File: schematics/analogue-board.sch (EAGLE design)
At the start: 81 parts, among them U1 L78S09

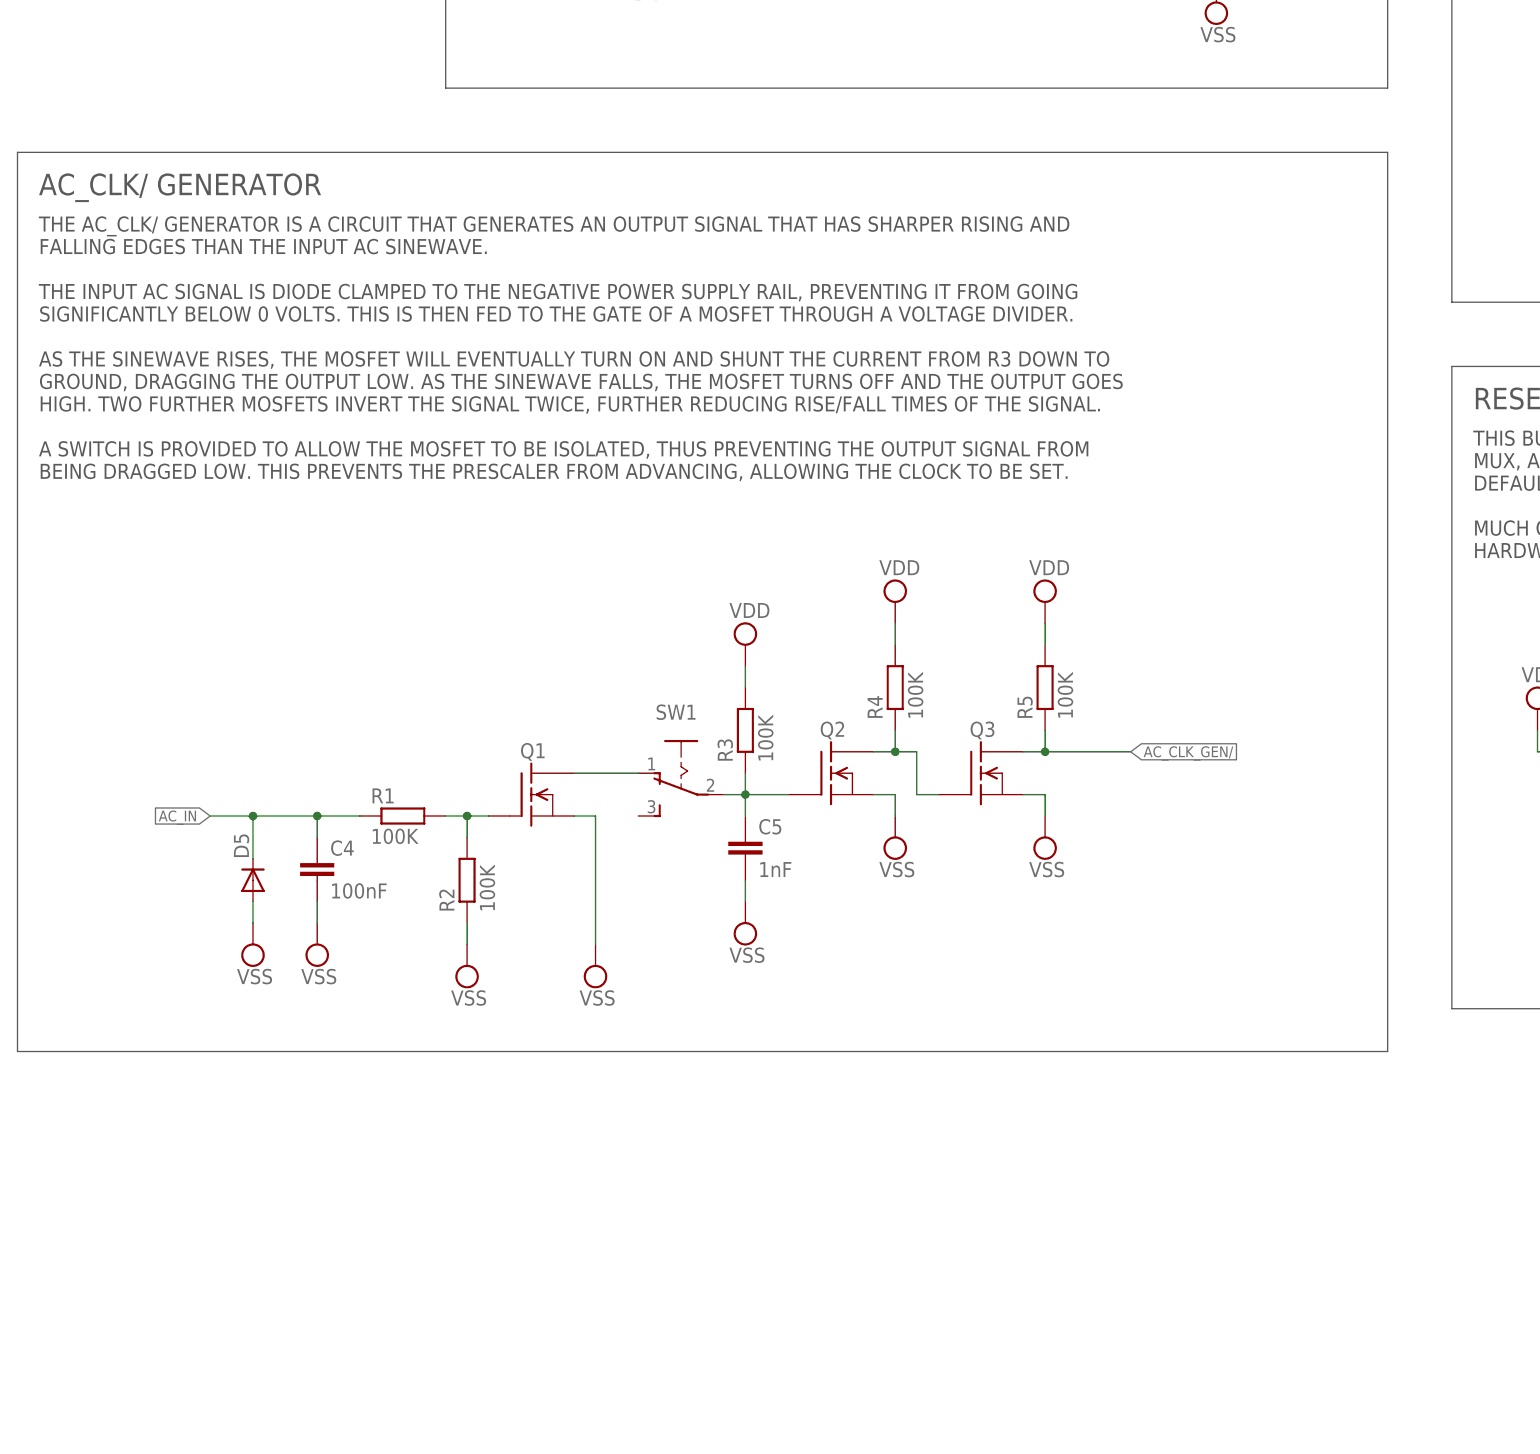
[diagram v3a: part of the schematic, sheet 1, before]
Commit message: Time module build (#7)
* Add design files (schematics) for time module.

* Upload files related to time module build.

Includes:

* revised analogue schematic to address a design fault
* C program used to collect offset statistics

* Rename directory for offset monitor program, its not a "script"

* Finalise README.md
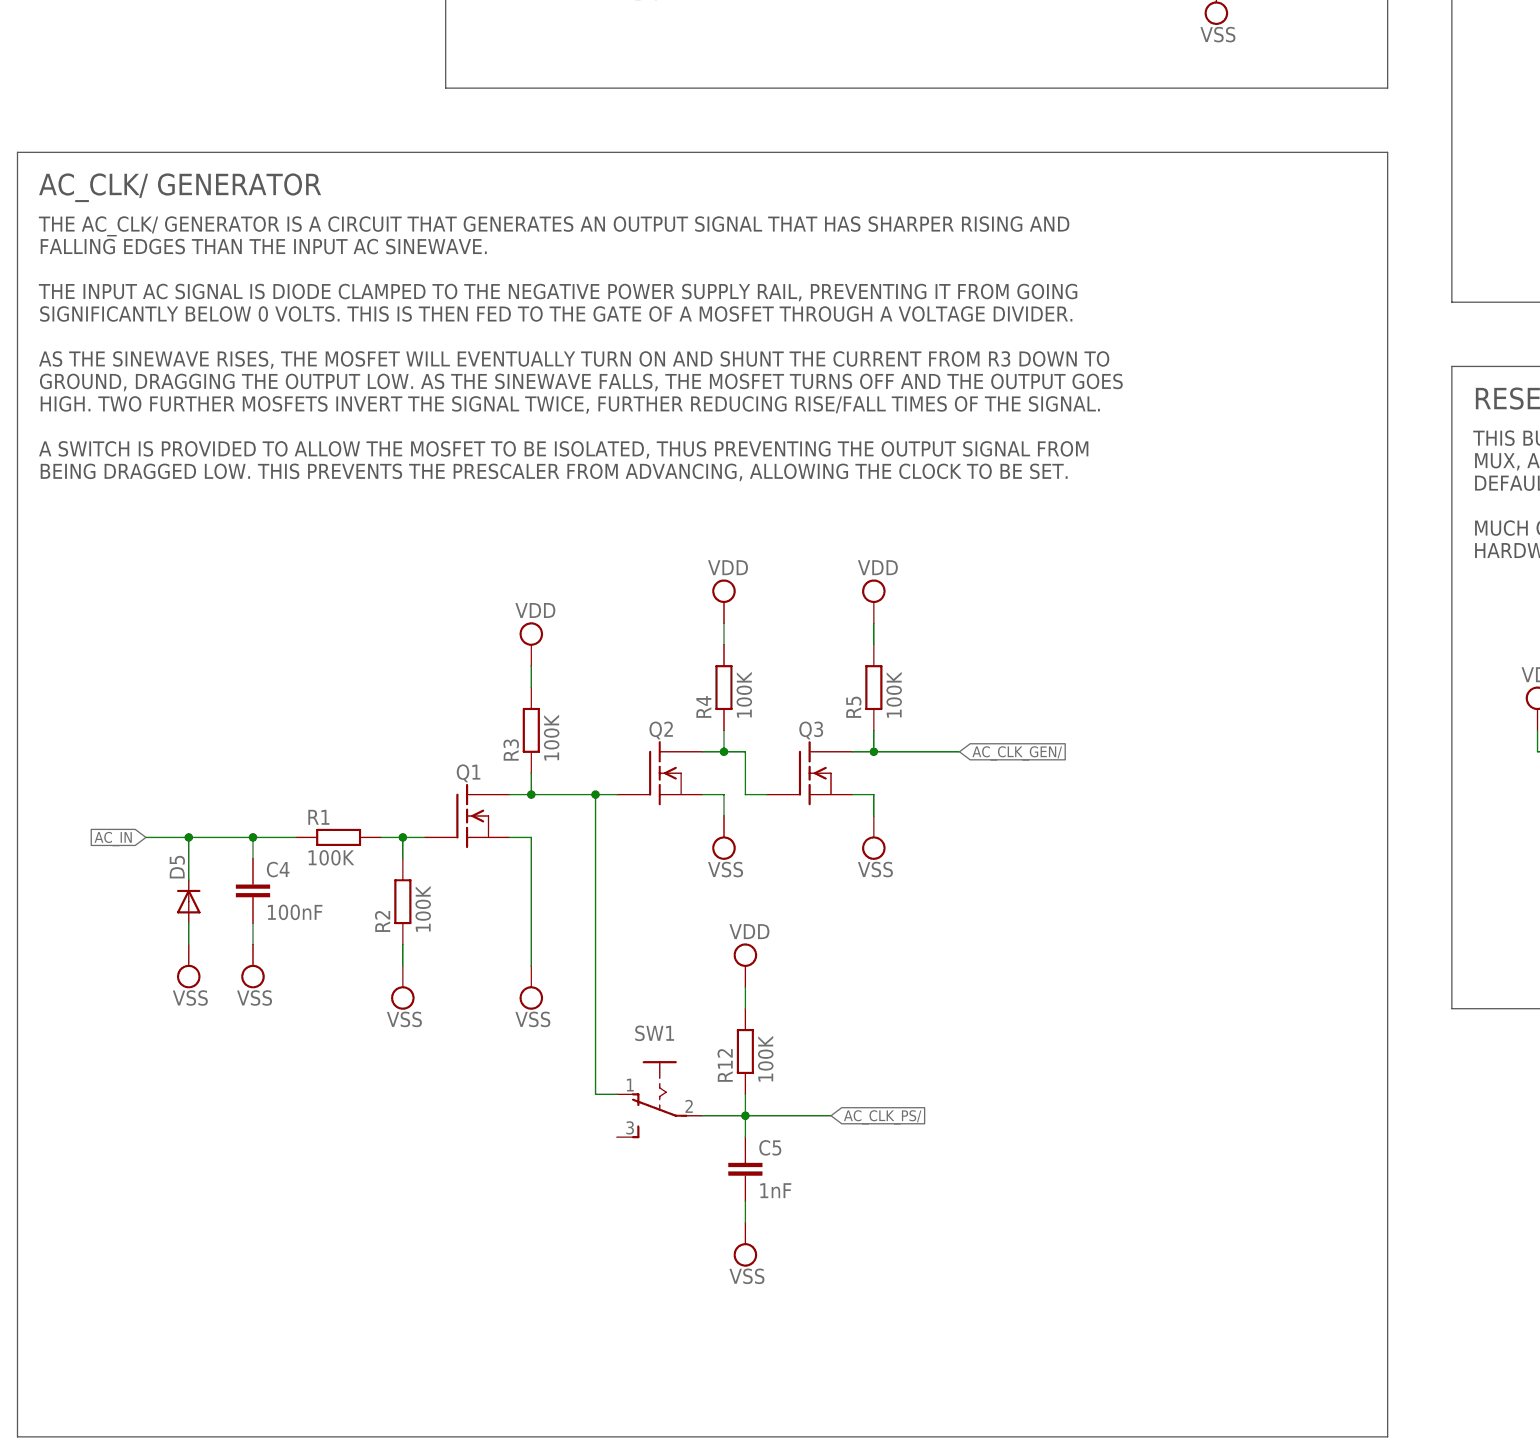
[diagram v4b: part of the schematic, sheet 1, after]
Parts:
- added R12: 100K, NOR gate clock:R-EU_0207/2V
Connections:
- removed net N$16: Q1.D, SW1.O
- new net AC_CLK_PS/: C5.1, GATE45.B, GATE5.A, R12.1, SW1.P
- net AC_CLK/: no longer GATE45.B, GATE5.A
- net N$1: now also Q1.D, SW1.O; no longer C5.1, SW1.P
- net VDD: now also R12.2
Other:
- moved on the sheet: C4, C5, D5, Q1, Q2, Q3, R1, R2, R3, R4, R5, SW1
